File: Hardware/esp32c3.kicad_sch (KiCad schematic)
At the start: 3 parts

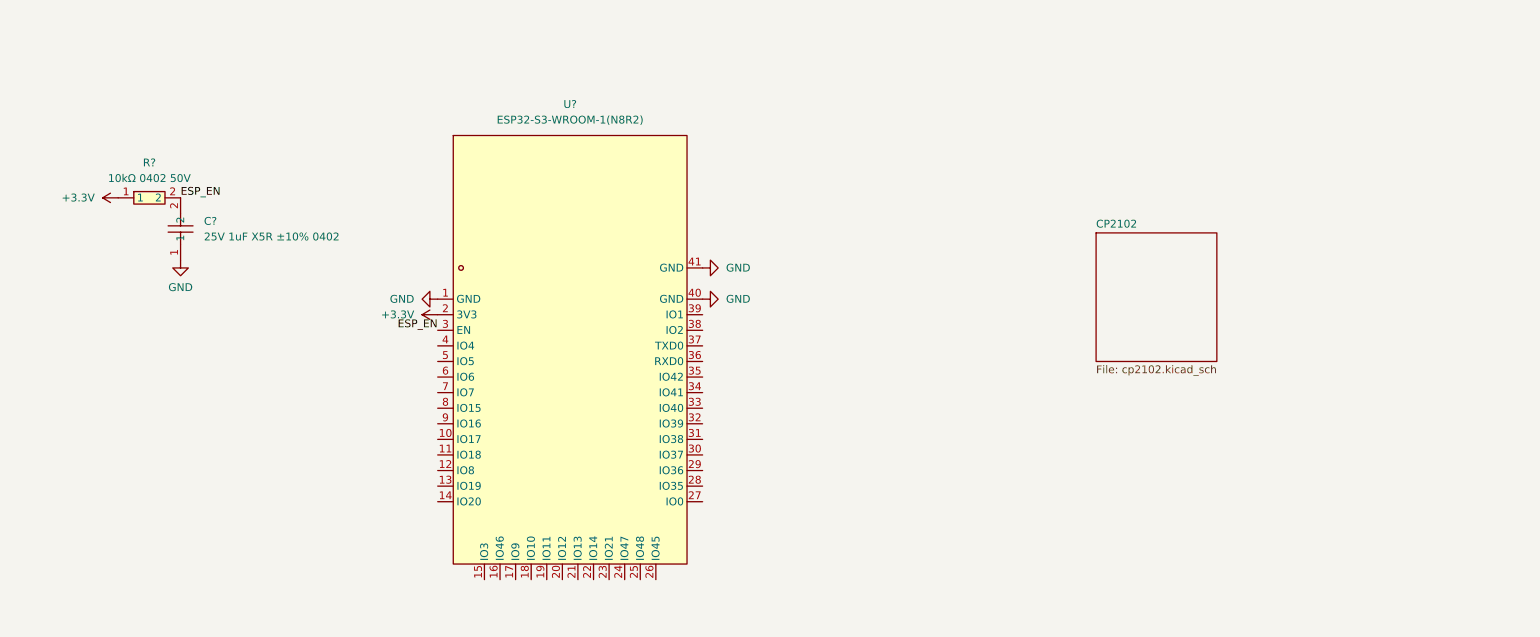
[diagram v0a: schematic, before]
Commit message: Added esp32 and bms
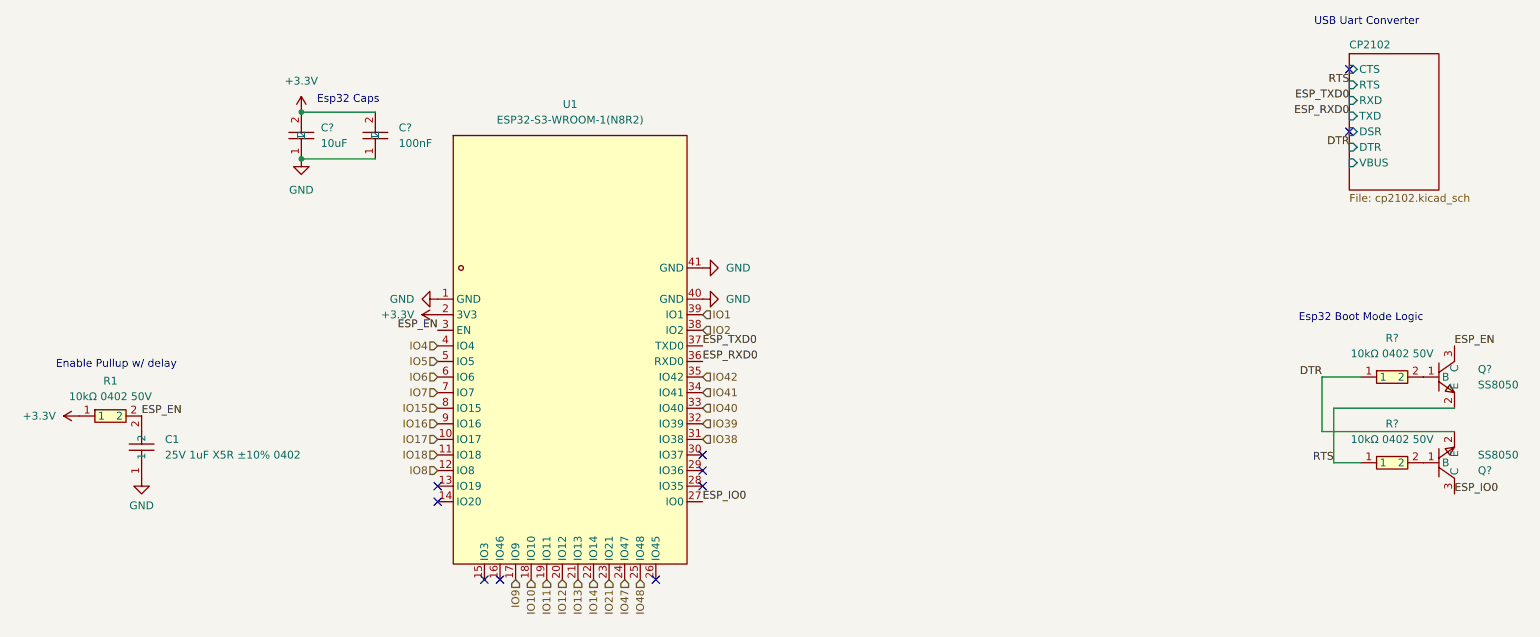
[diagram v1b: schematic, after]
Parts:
- added C?: 10uF, easyeda2kicad:C0402, symbol easyeda2kicad: 6.3V 10uF X5R ±20% 0402
- added C?: 100nF, easyeda2kicad:C0402_NEW, symbol easyeda2kicad:16V 100nF X7R ±10% 0402
- added Q? (x2): SS8050, easyeda2kicad:SOT-23-3_L2.9-W1.3-P1.90-LS2.4-BR, symbol easyeda2kicad:SS8050_C2150
- added R? (x2): 10kΩ 0402 50V, easyeda2kicad:R0402, symbol easyeda2kicad:10kΩ 0402 50V
- gave numbers to parts that had none: 3
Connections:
- net +3.3V: now also C?.2, C?.2
- net ESP_EN: now also Q?.3 (C)
- net GND: now also C?.1, C?.1
- net IO17: now reaches U1.10 (IO17)
- net IO18: now reaches U1.11 (IO18)
- net IO8: now reaches U1.12 (IO8)
- net IO9: now reaches U1.17 (IO9)
- net IO10: now reaches U1.18 (IO10)
- net IO11: now reaches U1.19 (IO11)
- net IO12: now reaches U1.20 (IO12)
- net IO13: now reaches U1.21 (IO13)
- net IO14: now reaches U1.22 (IO14)
- net IO21: now reaches U1.23 (IO21)
- net IO47: now reaches U1.24 (IO47)
- net IO48: now reaches U1.25 (IO48)
- net ESP_IO0: now reaches U1.27 (IO0)
- net ESP_IO0: now also Q?.3 (C)
- net IO38: now reaches U1.31 (IO38)
- net IO39: now reaches U1.32 (IO39)
- net IO40: now reaches U1.33 (IO40)
- net IO41: now reaches U1.34 (IO41)
- net IO42: now reaches U1.35 (IO42)
- net ESP_RXD0: now reaches U1.36 (RXD0)
- net ESP_TXD0: now reaches U1.37 (TXD0)
- net IO2: now reaches U1.38 (IO2)
- net IO1: now reaches U1.39 (IO1)
- net IO4: now reaches U1.4 (IO4)
- net IO5: now reaches U1.5 (IO5)
- net IO6: now reaches U1.6 (IO6)
- net IO7: now reaches U1.7 (IO7)
- net IO15: now reaches U1.8 (IO15)
- net IO16: now reaches U1.9 (IO16)
- new net: Q?.1 (B), R?.2 (x2)
- new net DTR: Q?.2 (E), R?.1
- new net RTS: Q?.2 (E), R?.1
- no-connect marks 0 -> 10
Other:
- sheet CP2102 ports: added CTS, DSR, DTR, RTS, RXD, TXD, VBUS; removed none
- note added: "Enable Pullup w/ delay"
- note added: "Esp32 Boot Mode Logic"
- note added: "Esp32 Caps"
- note added: "USB Uart Converter"
- moved on the sheet: C1, R1
